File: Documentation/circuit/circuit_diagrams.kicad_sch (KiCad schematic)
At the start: 8 parts, among them SW1 RotaryEncoder_Switch, SW2 SW_Push, U1 ESP32-C3-XIAO, U2 ADXL345, U3 SSD1306 OLED

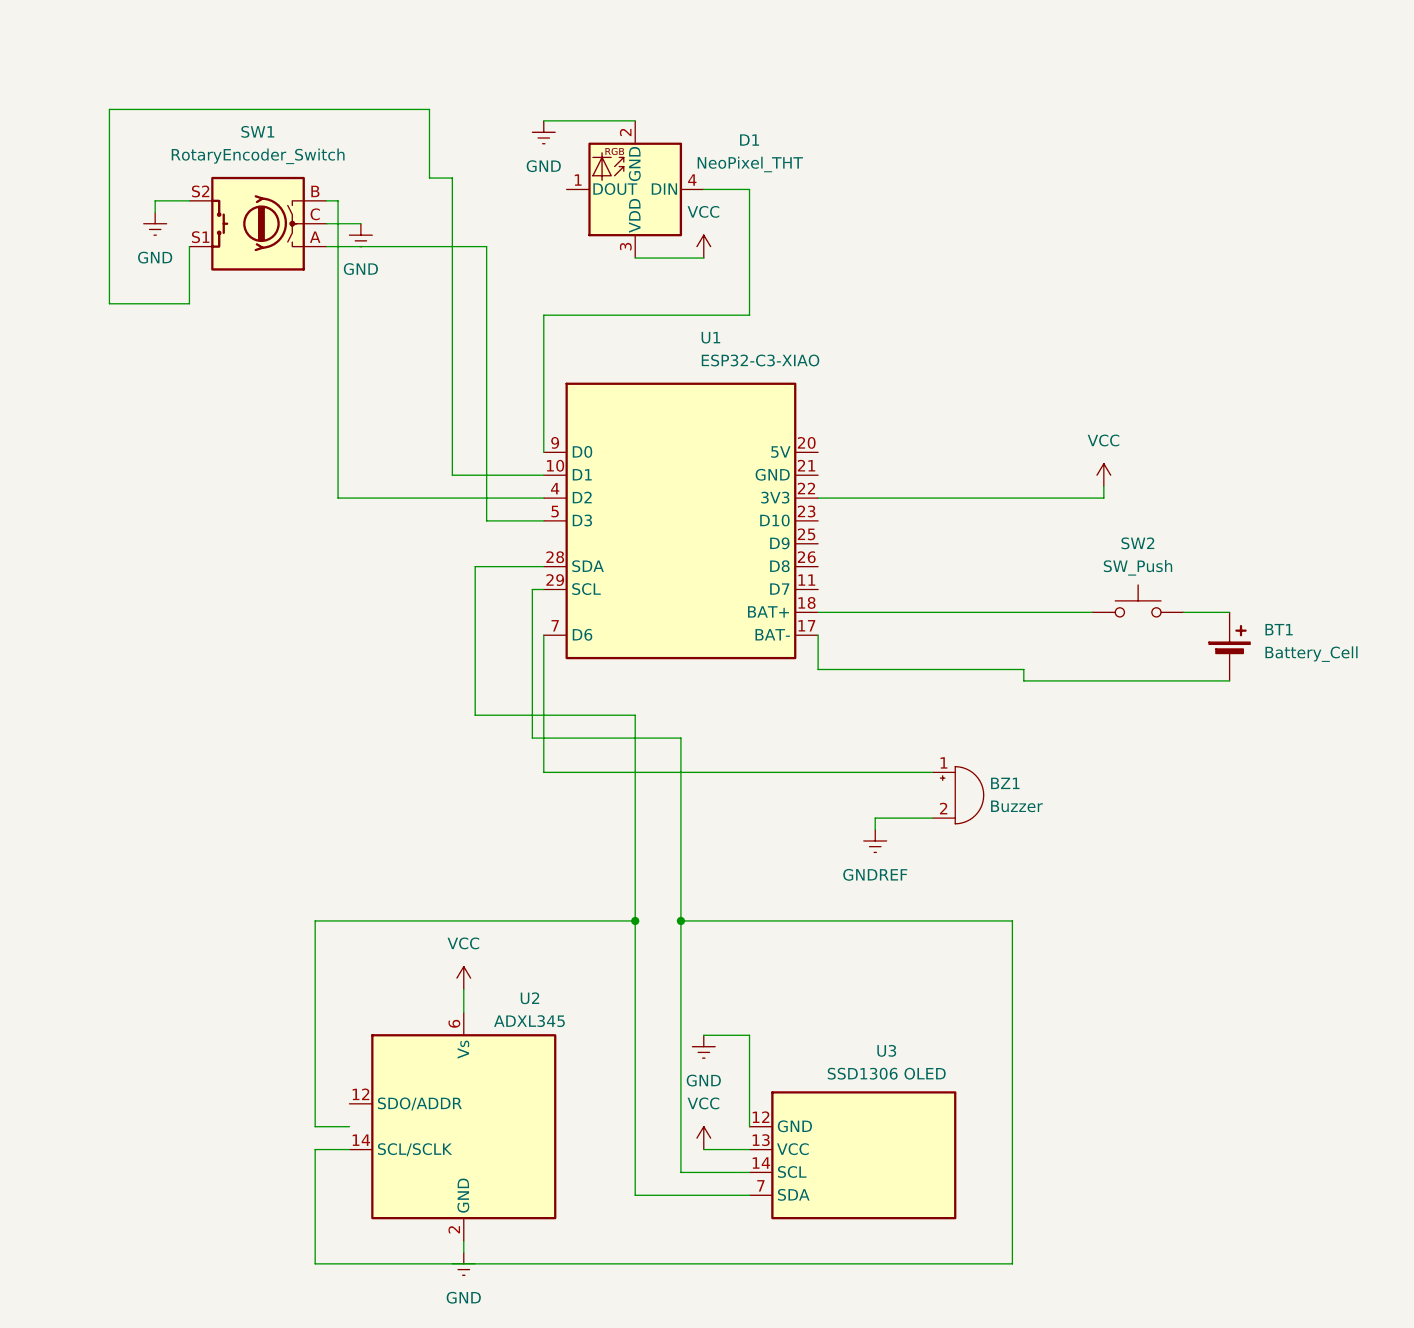
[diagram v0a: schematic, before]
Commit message: Reorganize documentation: separate circuit and system diagrams, update with latest files from assignment4-circuit
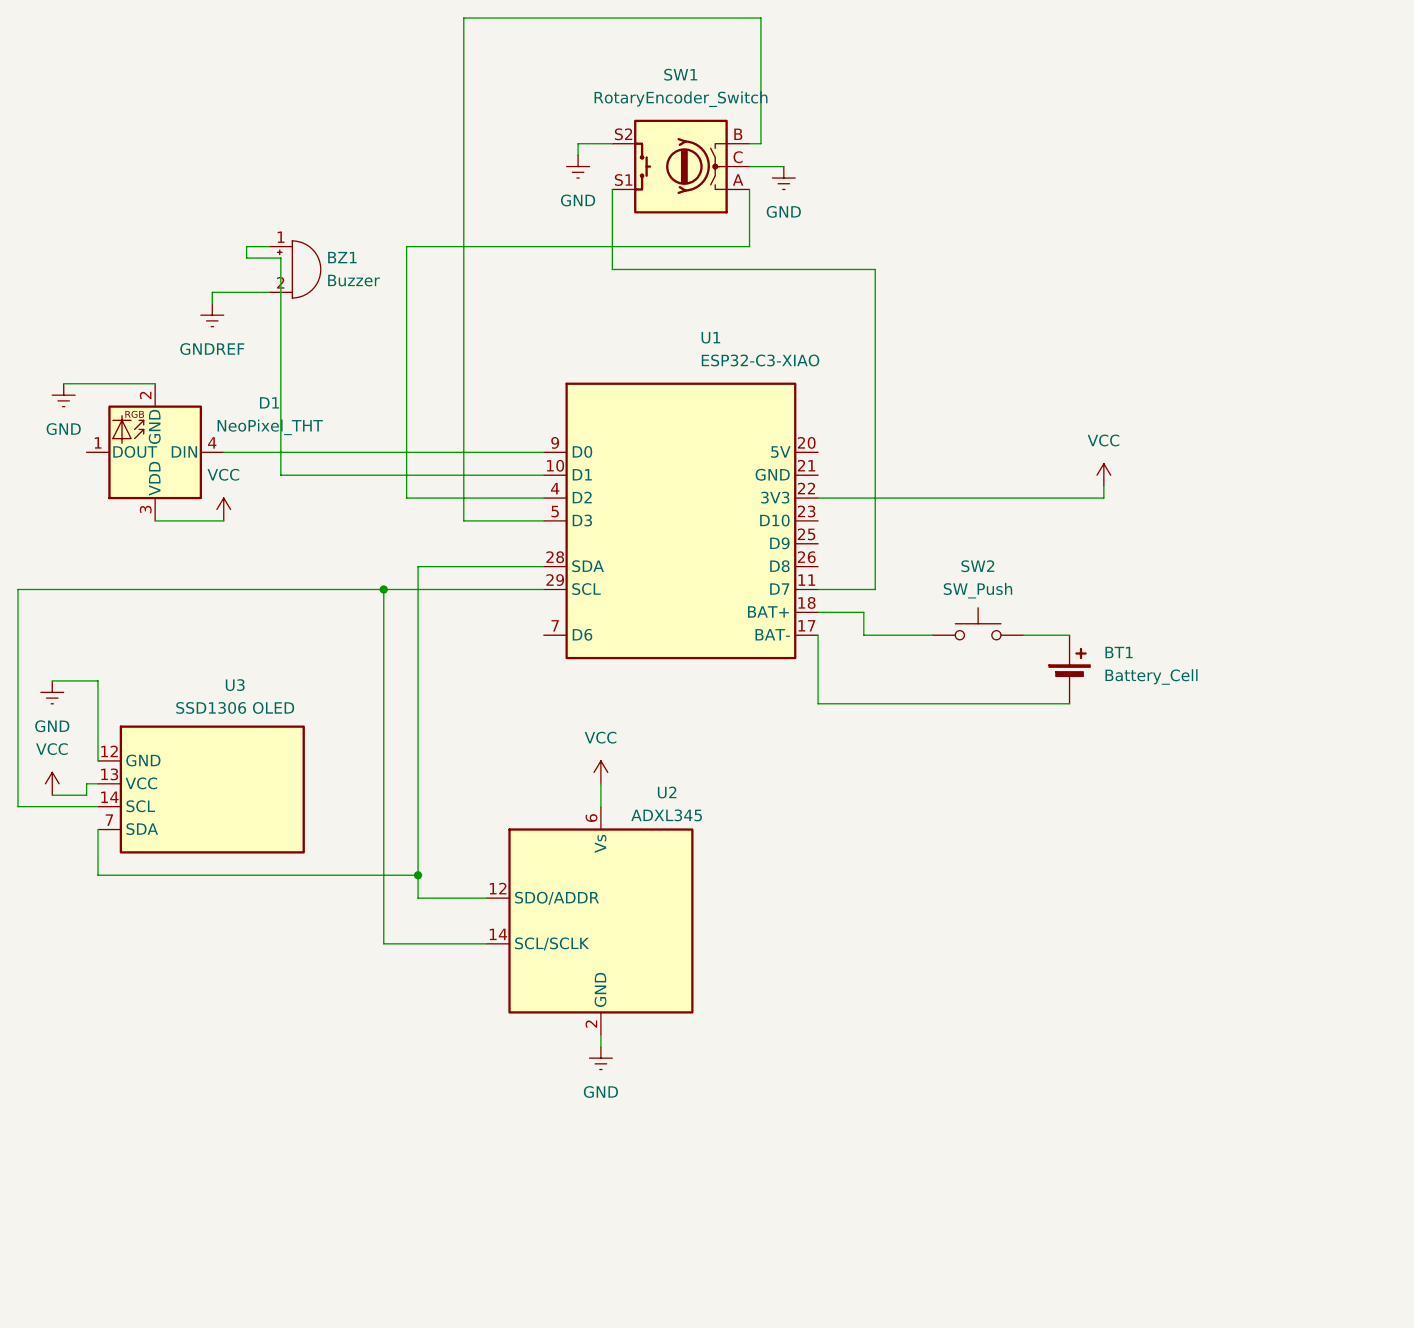
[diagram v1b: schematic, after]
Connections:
- net at BZ1.1 (+): now also U1.10 (D1); no longer U1.7 (D6)
- net at SW1.A: now also U1.4 (D2); no longer U1.5 (D3)
- net at SW1.B: now also U1.5 (D3); no longer U1.4 (D2)
- net at SW1.S1: now also U1.11 (D7); no longer U1.10 (D1)
- net at U1.28 (SDA), U3.7 (SDA): now also U2.12 (SDO/ADDR)
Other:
- moved on the sheet: BT1, BZ1, D1, SW1, SW2, U2, U3
